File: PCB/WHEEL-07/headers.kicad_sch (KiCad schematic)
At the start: 23 parts, among them IC4 NL27WZ14DTT1G, J10 BUTTON, J12 FRONT_PANEL, J2 SPI, J3 USART, J4 I2C, J5 PADDLE1, J6 PADDLE2, J7 BUTTON, J8 BUTTON, J9 BUTTON

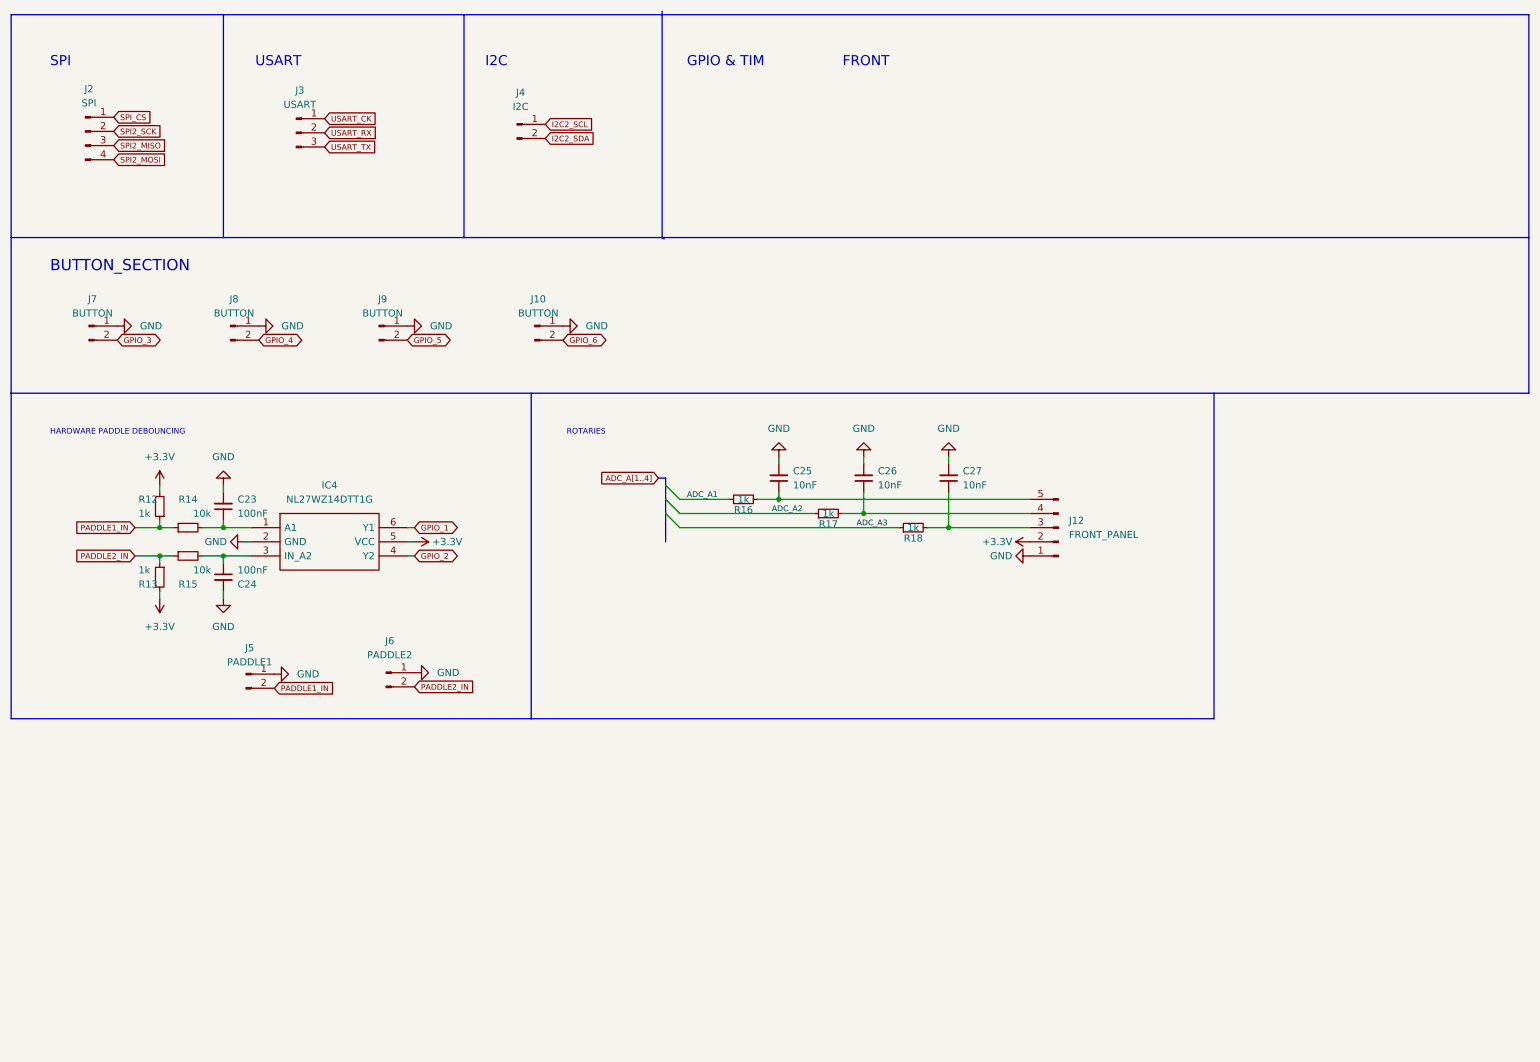
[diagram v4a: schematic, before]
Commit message: Modified schematics & assigned all footprints
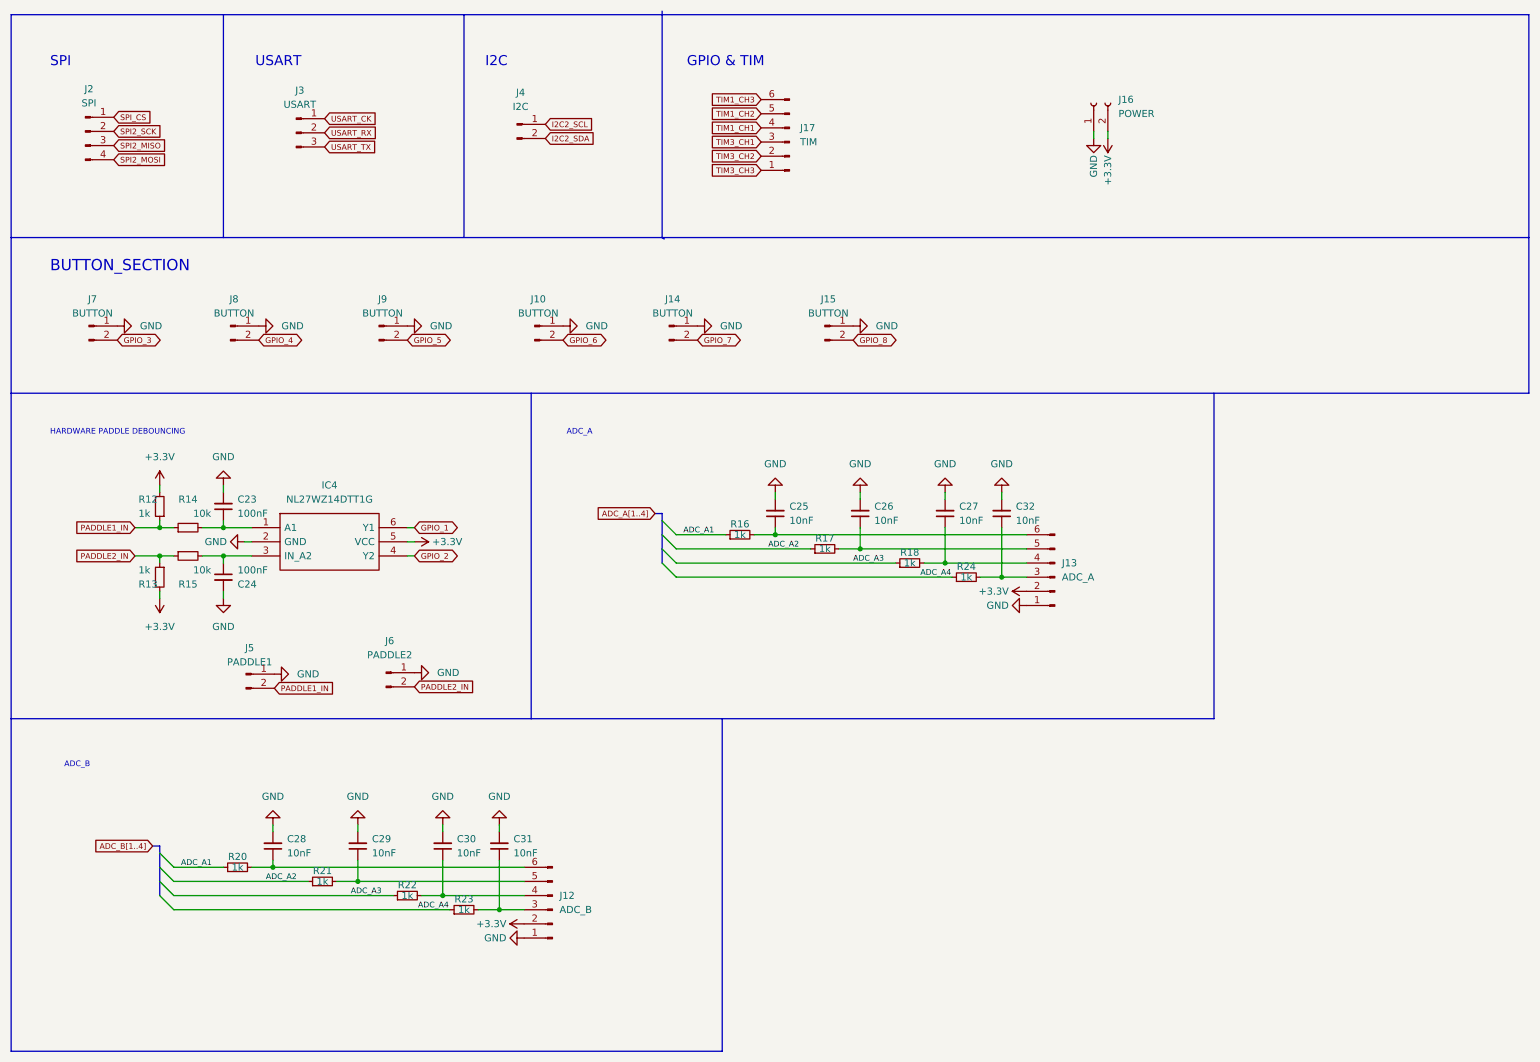
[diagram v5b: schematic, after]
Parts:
- removed J12: FRONT_PANEL, symbol Connector:Conn_01x05_Male
- added C28, C29, C30, C31, C32: 10nF, Capacitor_SMD:C_0402_1005Metric, symbol Device:C_Small
- added J12: ADC_B, Connector_Molex:Molex_PicoBlade_53047-0610_1x06_P1.25mm_Vertical, symbol Connector:Conn_01x06_Male
- added J13: ADC_A, Connector_Molex:Molex_PicoBlade_53047-0610_1x06_P1.25mm_Vertical, symbol Connector:Conn_01x06_Male
- added J14, J15: BUTTON, Connector_Molex:Molex_PicoBlade_53047-0210_1x02_P1.25mm_Vertical, symbol Connector:Conn_01x02_Male
- added J16: POWER, Connector_PinHeader_2.54mm:PinHeader_1x02_P2.54mm_Vertical, symbol Connector:Conn_01x02_Female
- added J17: TIM, Connector_Molex:Molex_PicoBlade_53047-0610_1x06_P1.25mm_Vertical, symbol Connector:Conn_01x06_Male
- added R20, R21, R22, R23, R24: 1k, Resistor_SMD:R_0402_1005Metric, symbol Device:R_Small
- C23, C24, C25, C26, C27: footprint (none) -> Capacitor_SMD:C_0402_1005Metric
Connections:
- net +3.3V: now also J12.2 (Pin_2), J13.2 (Pin_2), J16.2 (Pin_2)
- net ADC_A1: now also R20.1
- net ADC_A2: now also R21.1
- net ADC_A3: now also R22.1
- net GND: now also C28.2, C29.2, C30.2, C31.2, C32.2, J12.1 (Pin_1), J13.1 (Pin_1), J14.1 (Pin_1), J15.1 (Pin_1), J16.1 (Pin_1)
- net at C25.1, R16.2: now also J13.6 (Pin_6)
- net at C27.1, R18.2: now also J13.4 (Pin_4)
- net at C26.1, R17.2: now also J13.5 (Pin_5)
- new net: C32.1, J13.3 (Pin_3), R24.2
- new net: C31.1, J12.3 (Pin_3), R23.2
- new net: C30.1, J12.4 (Pin_4), R22.2
- new net: C29.1, J12.5 (Pin_5), R21.2
- new net: C28.1, J12.6 (Pin_6), R20.2
- new net ADC_A4: R23.1, R24.1
- new net GPIO_7: J14.2 (Pin_2)
- new net GPIO_8: J15.2 (Pin_2)
- new net TIM1_CH1: J17.4 (Pin_4)
- new net TIM1_CH2: J17.5 (Pin_5)
- new net TIM1_CH3: J17.6 (Pin_6)
- new net TIM3_CH1: J17.3 (Pin_3)
- new net TIM3_CH2: J17.2 (Pin_2)
- new net TIM3_CH3: J17.1 (Pin_1)
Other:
- note added: "ADC_A"
- note added: "ADC_B"
- note removed: "FRONT"
- note removed: "ROTARIES"
- moved on the sheet: C25, C26, C27, R16, R17, R18

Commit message: Changed connectors setup
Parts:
- removed J12: ADC_B, Connector_Molex:Molex_PicoBlade_53047-0610_1x06_P1.25mm_Vertical, symbol Connector:Conn_01x06_Male
- removed J13: ADC_A, Connector_Molex:Molex_PicoBlade_53047-0610_1x06_P1.25mm_Vertical, symbol Connector:Conn_01x06_Male
- added J12: Conn_01x10, Connector_Molex:Molex_PicoBlade_53047-1010_1x10_P1.25mm_Vertical, symbol Connector_Generic:Conn_01x10
- C23, C24, C25, C26, C27, C28, C29, C30, C31, C32: footprint Capacitor_SMD:C_0402_1005Metric -> Capacitor_SMD:C_0402_1005Metric_Pad0.74x0.62mm_HandSolder
- R12, R13, R14, R15, R16, R17, R18, R20, R21, R22, R23, R24: footprint Resistor_SMD:R_0402_1005Metric -> Resistor_SMD:R_0402_1005Metric_Pad0.72x0.64mm_HandSolder
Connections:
- net +3.3V: now also J12.1 (Pin_1)
- net ADC_A1: no longer R20.1
- net ADC_A2: no longer R21.1
- net ADC_A3: no longer R22.1
- net ADC_A4: no longer R23.1
- net GND: now also J12.2 (Pin_2)
- net at C32.1, R24.2: now also J12.7 (Pin_7)
- net at C31.1, R23.2: now also J12.3 (Pin_3)
- net at C30.1, R22.2: now also J12.4 (Pin_4)
- net at C29.1, R21.2: now also J12.5 (Pin_5)
- net at C28.1, R20.2: now also J12.6 (Pin_6)
- net at C25.1, R16.2: now also J12.10 (Pin_10)
- net at C27.1, R18.2: now also J12.8 (Pin_8)
- net at C26.1, R17.2: now also J12.9 (Pin_9)
- new net ADC_B1: R20.1
- new net ADC_B2: R21.1
- new net ADC_B3: R22.1
- new net ADC_B4: R23.1
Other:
- moved on the sheet: C28, C29, C30, C31, R20, R21, R22, R23

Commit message: Finished layout
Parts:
- removed J2: SPI, Connector_Molex:Molex_PicoBlade_53047-0310_1x03_P1.25mm_Vertical, symbol Connector:Conn_01x04_Male
- removed J3: USART, Connector_Molex:Molex_PicoBlade_53047-0310_1x03_P1.25mm_Vertical, symbol Connector:Conn_01x03_Male
- removed J4: I2C, Connector_Molex:Molex_PicoBlade_53047-0210_1x02_P1.25mm_Vertical, symbol Connector:Conn_01x02_Male
- removed J5: PADDLE1, Connector_Molex:Molex_PicoBlade_53047-0210_1x02_P1.25mm_Vertical, symbol Connector:Conn_01x02_Male
- removed J6: PADDLE2, Connector_Molex:Molex_PicoBlade_53047-0210_1x02_P1.25mm_Vertical, symbol Connector:Conn_01x02_Male
- added J2: Conn_01x06_Male, Connector_PinHeader_1.27mm:PinHeader_1x06_P1.27mm_Vertical, symbol Connector:Conn_01x06_Male
- added J5: Conn_01x04_Male, Connector_Molex:Molex_Micro-Latch_53254-0470_1x04_P2.00mm_Horizontal, symbol Connector:Conn_01x04_Male
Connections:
- net GND: now also J5.2 (Pin_2), J5.4 (Pin_4)
- net I2C2_SCL: now also J2.1 (Pin_1)
- net I2C2_SDA: now also J2.2 (Pin_2)
- net PADDLE1_IN: now also R13.1, R15.1, J5.1 (Pin_1); no longer R12.1, R14.1
- net PADDLE2_IN: now also R12.1, R14.1, J5.3 (Pin_3); no longer R13.1, R15.1
- net SPI2_MISO: now also J2.5 (Pin_5)
- net SPI2_MOSI: now also J2.6 (Pin_6)
- net SPI2_SCK: now also J2.4 (Pin_4)
- net SPI_CS: now also J2.3 (Pin_3)
- net TIM3_CH1: now also J17.1 (Pin_1); no longer J17.3 (Pin_3)
- net TIM3_CH3: now also J17.3 (Pin_3); no longer J17.1 (Pin_1)
